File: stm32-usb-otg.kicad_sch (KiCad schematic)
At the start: 34 parts

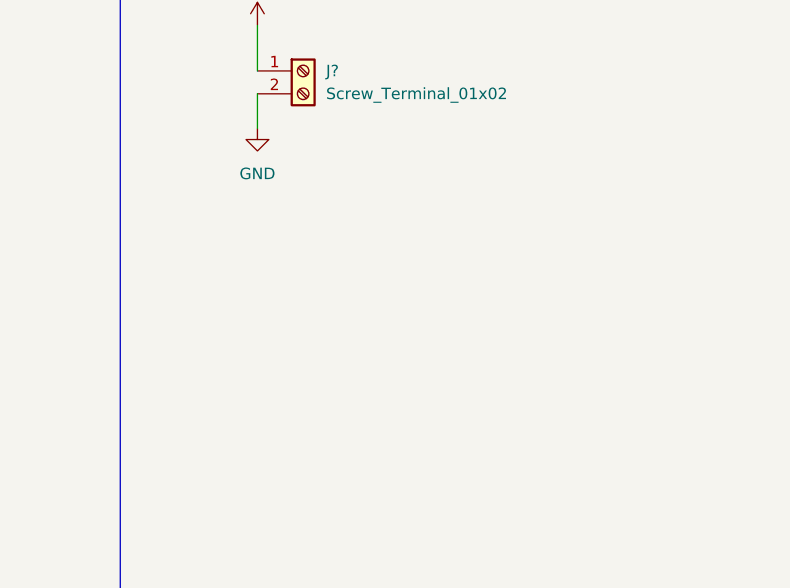
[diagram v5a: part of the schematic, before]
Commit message: Added SWD connector.
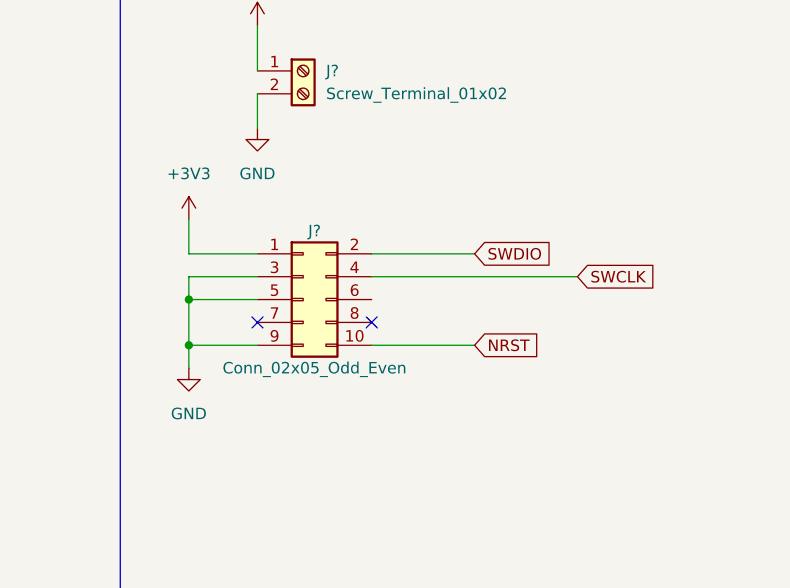
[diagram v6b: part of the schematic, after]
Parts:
- added J?: Conn_02x05_Odd_Even, symbol Connector_Generic:Conn_02x05_Odd_Even
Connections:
- net +3V3: now also J?.1 (Pin_1)
- net GND: now also J?.3 (Pin_3), J?.5 (Pin_5), J?.9 (Pin_9)
- net NRST: now also J?.10 (Pin_10)
- net SWDIO: now also J?.2 (Pin_2)
- new net SWCLK: J?.4 (Pin_4)
- no-connect marks 41 -> 43
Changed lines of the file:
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@@
   (junction (at 231.14 29.21) (diameter 0) (color 0 0 0 0)
   )
+  (junction (at 220.98 106.68) (diameter 0) (color 0 0 0 0)
+  )
   (junction (at 29.21 81.28) (diameter 0) (color 0 0 0 0)
   )
@@
   )
   (junction (at 125.73 88.9) (diameter 0) (color 0 0 0 0)
+  )
+  (junction (at 220.98 101.6) (diameter 0) (color 0 0 0 0)
   )
   (junction (at 38.1 81.28) (diameter 0) (color 0 0 0 0)
@@
   (no_connect (at 140.97 143.51))
   (no_connect (at 140.97 144.78))
+  (no_connect (at 228.6 104.14))
+  (no_connect (at 241.3 104.14))
   (wire (pts (xy 99.06 115.57) (xy 99.06 111.76))
     (stroke (width 0) (type default) (color 0 0 0 0))
@@
     (stroke (width 0) (type default) (color 0 0 0 0))
   )
+  (wire (pts (xy 228.6 99.06) (xy 220.98 99.06))
+    (stroke (width 0) (type default) (color 0 0 0 0))
+  )
+  (wire (pts (xy 220.98 96.52) (xy 228.6 96.52))
+    (stroke (width 0) (type default) (color 0 0 0 0))
+  )
   (polyline (pts (xy 213.36 59.69) (xy 213.36 198.12))
     (stroke (width 0) (type default) (color 0 0 0 0))
@@
     (stroke (width 0) (type default) (color 0 0 0 0))
   )
+  (wire (pts (xy 228.6 101.6) (xy 220.98 101.6))
+    (stroke (width 0) (type default) (color 0 0 0 0))
+  )
   (wire (pts (xy 219.71 44.45) (xy 219.71 52.07))
     (stroke (width 0) (type default) (color 0 0 0 0))
@@
     (stroke (width 0) (type default) (color 0 0 0 0))
   )
+  (wire (pts (xy 220.98 101.6) (xy 220.98 106.68))
+    (stroke (width 0) (type default) (color 0 0 0 0))
+  )
   (wire (pts (xy 102.87 76.2) (xy 102.87 78.74))
     (stroke (width 0) (type default) (color 0 0 0 0))
@@
     (stroke (width 0) (type default) (color 0 0 0 0))
   )
+  (wire (pts (xy 220.98 106.68) (xy 220.98 109.22))
+    (stroke (width 0) (type default) (color 0 0 0 0))
+  )
   (wire (pts (xy 67.31 19.05) (xy 67.31 34.29))
     (stroke (width 0) (type default) (color 0 0 0 0))
@@
     (stroke (width 0) (type default) (color 0 0 0 0))
   )
+  (wire (pts (xy 220.98 92.71) (xy 220.98 96.52))
+    (stroke (width 0) (type default) (color 0 0 0 0))
+  )
   (wire (pts (xy 55.88 119.38) (xy 55.88 110.49))
     (stroke (width 0) (type default) (color 0 0 0 0))
@@
     (stroke (width 0) (type default) (color 0 0 0 0))
   )
+  (wire (pts (xy 241.3 106.68) (xy 252.73 106.68))
+    (stroke (width 0) (type default) (color 0 0 0 0))
+  )
   (wire (pts (xy 55.88 146.05) (xy 55.88 142.24))
     (stroke (width 0) (type default) (color 0 0 0 0))
@@
     (stroke (width 0) (type default) (color 0 0 0 0))
   )
+  (wire (pts (xy 241.3 99.06) (xy 264.16 99.06))
+    (stroke (width 0) (type default) (color 0 0 0 0))
+  )
   (wire (pts (xy 24.13 121.92) (xy 35.56 121.92))
     (stroke (width 0) (type default) (color 0 0 0 0))
@@
     (stroke (width 0) (type default) (color 0 0 0 0))
   )
+  (wire (pts (xy 241.3 96.52) (xy 252.73 96.52))
+    (stroke (width 0) (type default) (color 0 0 0 0))
+  )
   (wire (pts (xy 228.6 71.12) (xy 228.6 76.2))
     (stroke (width 0) (type default) (color 0 0 0 0))
@@
     (stroke (width 0) (type default) (color 0 0 0 0))
   )
+  (wire (pts (xy 228.6 106.68) (xy 220.98 106.68))
+    (stroke (width 0) (type default) (color 0 0 0 0))
+  )
   (wire (pts (xy 86.36 124.46) (xy 105.41 124.46))
+    (stroke (width 0) (type default) (color 0 0 0 0))
+  )
+  (wire (pts (xy 220.98 99.06) (xy 220.98 101.6))
     (stroke (width 0) (type default) (color 0 0 0 0))
   )
@@
     )
   )
+  (global_label "NRST" (shape input) (at 252.73 106.68 0) (fields_autoplaced)
+    (effects (font (size 1.27 1.27)) (justify left))
+    (property "Intersheet References" "${INTERSHEET_REFS}" (id 0) (at 259.9207 106.6006 0)
+      (effects (font (size 1.27 1.27)) (justify left) hide)
+    )
+  )
   (global_label "BUCK_SW" (shape input) (at 165.1 29.21 0) (fields_autoplaced)
     (effects (font (size 1.27 1.27)) (justify left))
@@
     )
   )
+  (global_label "SWDIO" (shape input) (at 252.73 96.52 0) (fields_autoplaced)
+    (effects (font (size 1.27 1.27)) (justify left))
+    (property "Intersheet References" "${INTERSHEET_REFS}" (id 0) (at 261.0093 96.4406 0)
+      (effects (font (size 1.27 1.27)) (justify left) hide)
+    )
+  )
   (global_label "LED_STATUS" (shape input) (at 140.97 99.06 0) (fields_autoplaced)
     (effects (font (size 1.27 1.27)) (justify left))
@@
     )
   )
+  (global_label "SWCLK" (shape input) (at 264.16 99.06 0) (fields_autoplaced)
+    (effects (font (size 1.27 1.27)) (justify left))
+    (property "Intersheet References" "${INTERSHEET_REFS}" (id 0) (at 272.8021 98.9806 0)
+      (effects (font (size 1.27 1.27)) (justify left) hide)
+    )
+  )
   (global_label "BUCK_IN" (shape input) (at 40.64 39.37 0) (fields_autoplaced)
     (effects (font (size 1.27 1.27)) (justify left))
@@
     (pin "1")
   )
+  (symbol (lib_id "Connector_Generic:Conn_02x05_Odd_Even") (at 233.68 101.6 0) (unit 1)
+    (in_bom yes) (on_board yes)
+    (property "Reference" "J?" (id 0) (at 234.95 93.98 0))
+    (property "Value" "Conn_02x05_Odd_Even" (id 1) (at 234.95 109.22 0))
+    (property "Footprint" "" (id 2) (at 233.68 101.6 0)
+      (effects (font (size 1.27 1.27)) hide)
+    )
+    (property "Datasheet" "~" (id 3) (at 233.68 101.6 0)
+      (effects (font (size 1.27 1.27)) hide)
+    )
+    (pin "1")
+    (pin "10")
+    (pin "2")
+    (pin "3")
+    (pin "4")
+    (pin "5")
+    (pin "6")
+    (pin "7")
+    (pin "8")
+    (pin "9")
+  )
   (symbol (lib_id "power:GND") (at 45.72 165.1 0) (unit 1)
     (in_bom yes) (on_board yes) (fields_autoplaced)
@@
     (pin "1")
   )
+  (symbol (lib_id "power:GND") (at 220.98 109.22 0) (unit 1)
+    (in_bom yes) (on_board yes) (fields_autoplaced)
+    (property "Reference" "#PWR?" (id 0) (at 220.98 115.57 0)
+      (effects (font (size 1.27 1.27)) hide)
+    )
+    (property "Value" "GND" (id 1) (at 220.98 114.3 0))
+    (property "Footprint" "" (id 2) (at 220.98 109.22 0)
+      (effects (font (size 1.27 1.27)) hide)
+    )
+    (property "Datasheet" "" (id 3) (at 220.98 109.22 0)
+      (effects (font (size 1.27 1.27)) hide)
+    )
+    (pin "1")
+  )
   (symbol (lib_id "Device:R_Small_US") (at 231.14 34.29 0) (unit 1)
     (in_bom yes) (on_board yes) (fields_autoplaced)
@@
     (pin "1")
     (pin "2")
+  )
+  (symbol (lib_id "power:+3V3") (at 220.98 92.71 0) (unit 1)
+    (in_bom yes) (on_board yes) (fields_autoplaced)
+    (property "Reference" "#PWR?" (id 0) (at 220.98 96.52 0)
+      (effects (font (size 1.27 1.27)) hide)
+    )
+    (property "Value" "+3V3" (id 1) (at 220.98 87.63 0))
+    (property "Footprint" "" (id 2) (at 220.98 92.71 0)
+      (effects (font (size 1.27 1.27)) hide)
+    )
+    (property "Datasheet" "" (id 3) (at 220.98 92.71 0)
+      (effects (font (size 1.27 1.27)) hide)
+    )
+    (pin "1")
   )
   (symbol (lib_id "Switch:SW_SPDT") (at 50.8 121.92 0) (unit 1)
@@
       (reference "#PWR?") (unit 1) (value "+12V") (footprint "")
     )
+    (path "/48405fc5-2c51-4b58-bef3-eca7a10b6fae"
+      (reference "#PWR?") (unit 1) (value "GND") (footprint "")
+    )
+    (path "/4eb25cd7-5e93-403d-9c63-d334e8afc126"
+      (reference "#PWR?") (unit 1) (value "+3V3") (footprint "")
+    )
     (path "/aab184e6-7f4d-40db-9212-1d2496e8c4c5"
       (reference "#PWR?") (unit 1) (value "GND") (footprint "")
@@
       (reference "FB?") (unit 1) (value "FerriteBead_Small") (footprint "")
     )
+    (path "/0b7e1823-6eac-4b15-b3be-85dcf20f7791"
+      (reference "J?") (unit 1) (value "Conn_02x05_Odd_Even") (footprint "")
+    )
     (path "/1fc4ac31-c5c2-4205-ae19-4c4a902842a7"

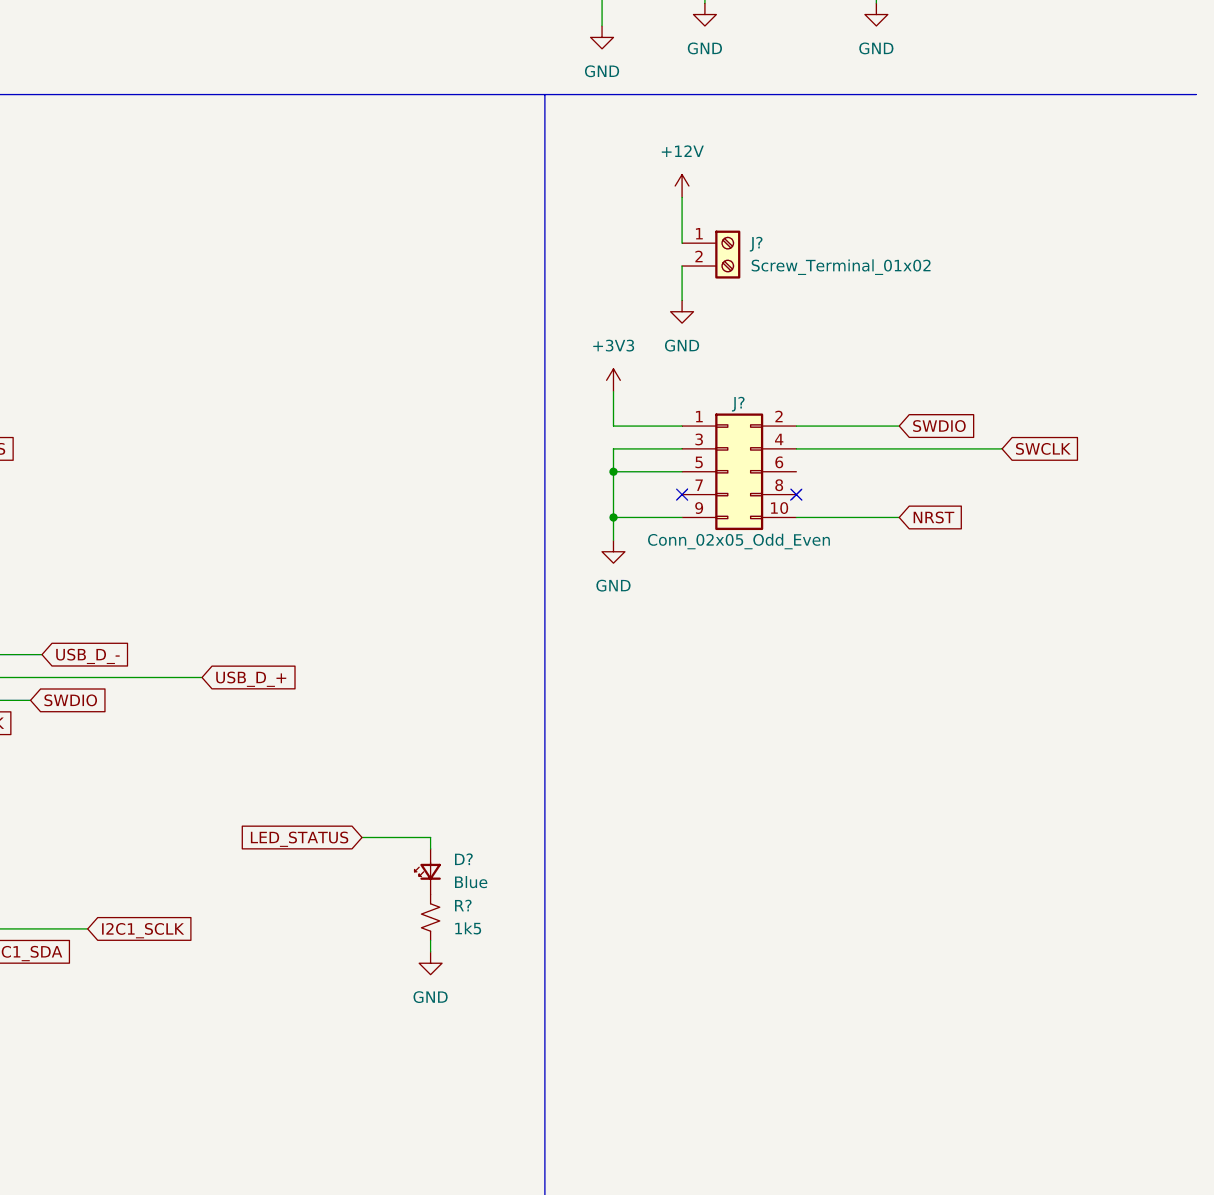
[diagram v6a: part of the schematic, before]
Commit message: Add UART, I2C connectors.
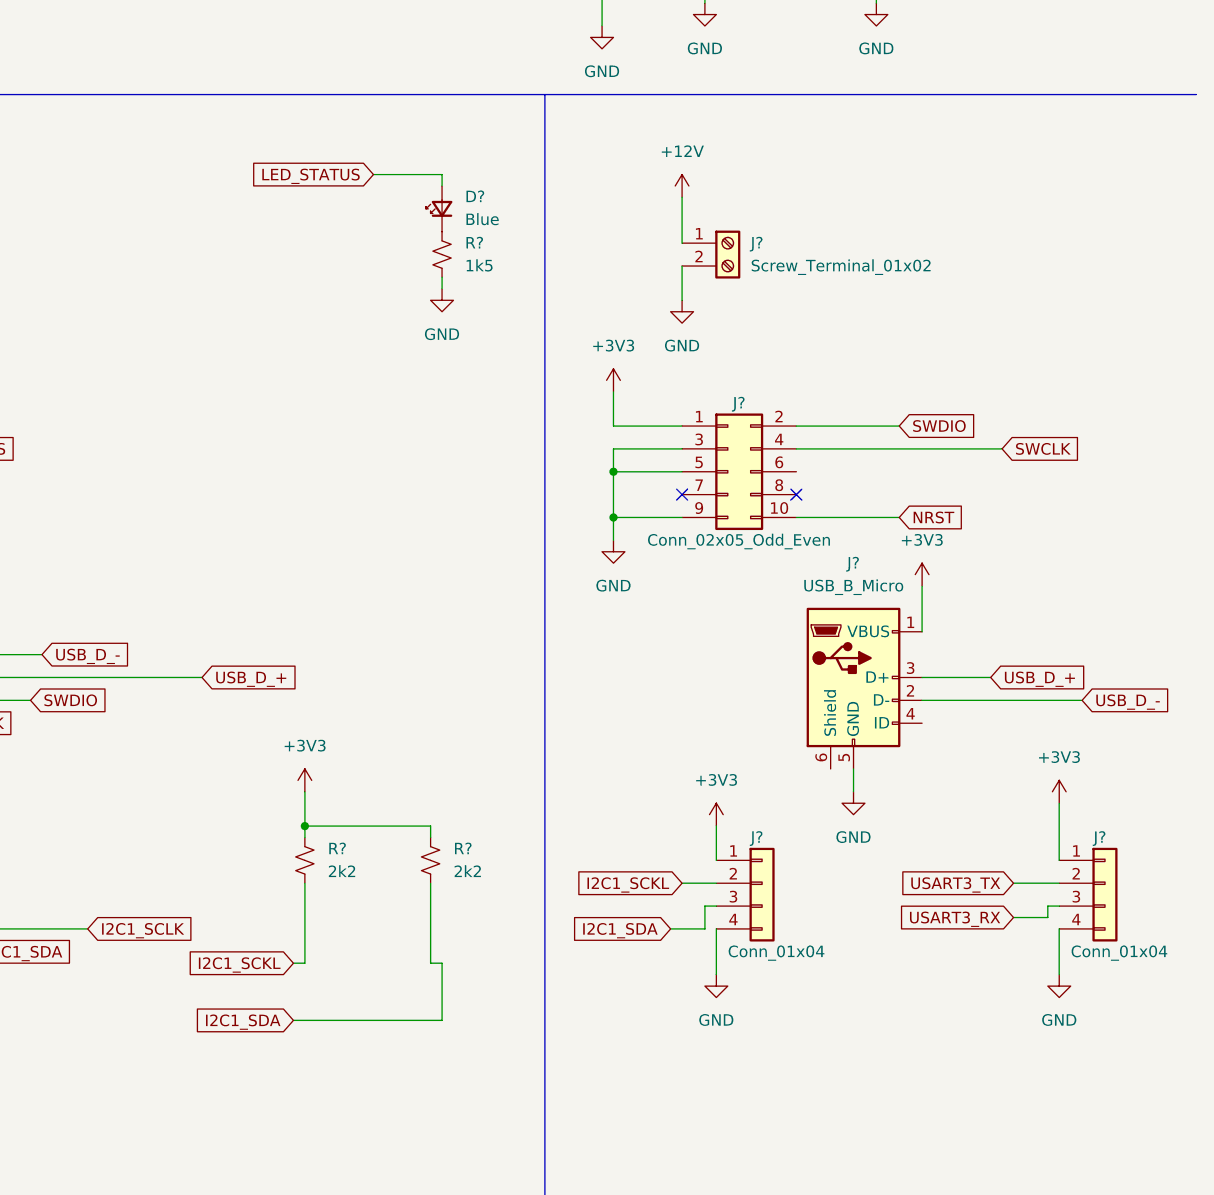
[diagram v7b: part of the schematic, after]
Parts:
- added J? (x2): Conn_01x04, symbol Connector_Generic:Conn_01x04
- added J?: USB_B_Micro, symbol Connector:USB_B_Micro
- added R? (x2): 2k2, symbol Device:R_Small_US
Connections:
- net +3V3: now also J?.1 (Pin_1), J?.1 (Pin_1), J?.1 (VBUS), R?.1, R?.1
- net GND: now also J?.4 (Pin_4), J?.4 (Pin_4), J?.5 (GND)
- net I2C1_SDA: now also J?.3 (Pin_3), R?.2
- net USART3_RX: now also J?.3 (Pin_3)
- net USART3_TX: now also J?.2 (Pin_2)
- net USB_D_+: now also J?.3 (D+)
- net USB_D_-: now also J?.2 (D-)
- new net I2C1_SCKL: J?.2 (Pin_2), R?.2
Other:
- moved on the sheet: D?, R?
